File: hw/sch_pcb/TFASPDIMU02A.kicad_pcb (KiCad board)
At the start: 2 copper layers, 30 x 15 mm, 39 parts, among them J1 SM04B-GHS-TB, M1 HOLE_TF, M2 HOLE_TF, M3 HOLE_TF, M7 HOLE_TF, U1 SDP3x, U2 ICM-20948, U3 TCA9617A, U4 MIC5504-3.3YM5-TR, U5 MIC5504-1.8YM5-TR, U6 TCA9617A

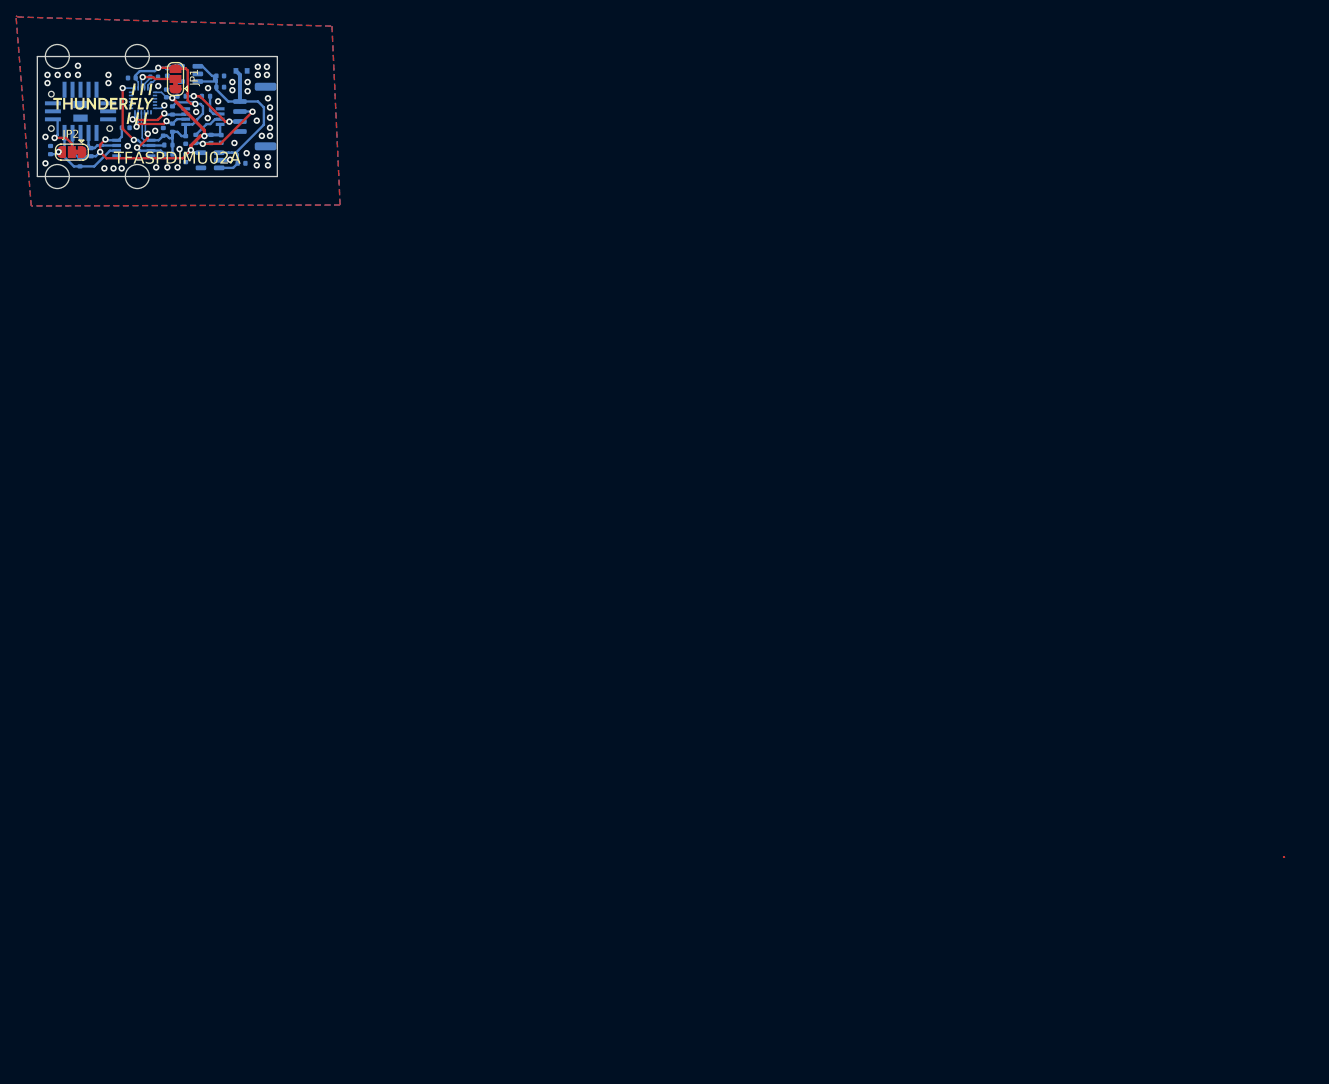
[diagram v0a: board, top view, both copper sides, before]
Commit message: Update title block Move PCB to center of page Mark magnetometer orientation in silkscreen
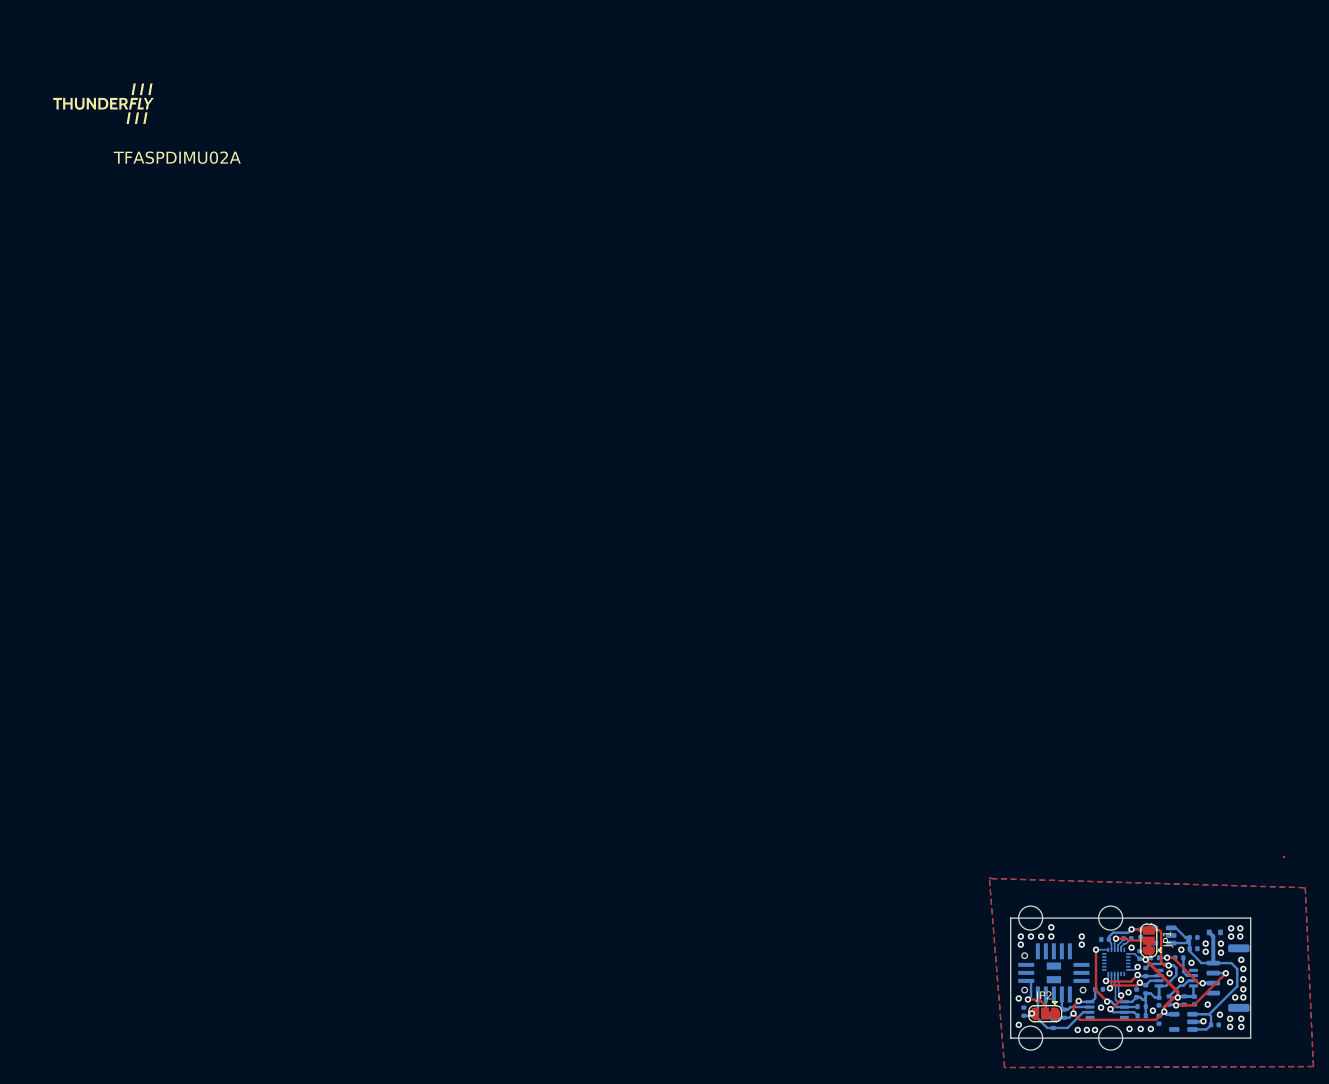
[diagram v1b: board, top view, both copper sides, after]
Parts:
- moved C1 162.5 mm to (126.6, 104.3)
- moved C10 162.5 mm to (132.7, 101.6)
- moved C12 162.5 mm to (140.2, 103.1)
- moved C13 162.5 mm to (144.7, 103.0)
- moved C2 162.5 mm to (133.5, 95.4)
- moved C7 162.5 mm to (140.2, 105.4)
- moved C8 162.5 mm to (137.9, 94.6)
- moved J1 162.5 mm to (148.8, 100.2)
- moved JP1 162.5 mm to (138.9, 95.5)
- moved JP2 162.5 mm to (126.0, 104.6)
- moved M1 162.5 mm to (134.2, 107.7)
- moved M2 162.5 mm to (124.2, 107.7)
- moved M3 162.5 mm to (124.2, 92.7)
- moved M7 162.5 mm to (134.2, 92.7)
- moved R10 162.5 mm to (123.3, 104.4)
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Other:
- board text added: "Y | X-Z"
